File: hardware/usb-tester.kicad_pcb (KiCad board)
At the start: 2 copper layers, 32 parts, among them J1 TARGET, J10 Target 1, J11 USB1, J12 SWD2, J13 Target 2, J14 USB2, J15 SWD3, J16 Target 3, J17 USB3, J2 Comm, J3 CommLA, J4 PowerMon, J5 Upstream, J6 SWD0, J7 Target 0, J8 USB0, J9 SWD1, U1 TLV1117-33, U2 STMPS2151STR, U3 USBLC6-2SC6, U4 CD74HC4067SM, U5 4514, U6 FSUSB30MUX, U7 FSUSB30MUX

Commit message: WIP main board layout
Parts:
- R1, R2, R3, R4, R5, U5: moved to B.Cu
- moved R3 101.2 mm to (25.4, 125.7), turned to 180 degrees
- moved R5 93.2 mm to (25.4, 130.8)
- moved R4 84.1 mm to (25.4, 128.3), turned to 180 degrees
- moved R2 66.9 mm to (25.4, 113.0)
- moved J2 65.5 mm to (21.6, 108.0)
- moved J3 64.0 mm to (19.1, 108.0)
- moved U4 63.0 mm to (50.8, 125.9), turned to 180 degrees
- moved R1 60.4 mm to (25.4, 110.5)
- moved U5 54.8 mm to (55.2, 118.1)
- moved JP1 53.4 mm to (95.1, 60.1)
- moved C2 49.4 mm to (106.8, 58.2), turned to 180 degrees
- moved J14 35.8 mm to (66.0, 128.3)
- moved C1 33.4 mm to (102.5, 70.6)
- moved J4 32.4 mm to (117.1, 67.8)
- moved J17 30.8 mm to (81.3, 128.3)
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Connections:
- net Net-(C1-Pad1) renamed /VIN
- J1 pad 4: (no net) -> Net-(J1-Pad4)
- J5 pad 1: /USB_D+ -> GND
- J5 pad 3: GND -> /USB_D+
- U3 pad 1: /USB_D- -> /USB_D+
- U3 pad 3: /USB_D+ -> /USB_D-
- U3 pad 4: Net-(J1-Pad3) -> Net-(J1-Pad2)
- U3 pad 6: Net-(J1-Pad2) -> Net-(J1-Pad3)
- U4 pad 16: (no net) -> Net-(U4-Pad16)
- U4 pad 17: (no net) -> Net-(U4-Pad17)
- U4 pad 18: (no net) -> Net-(U4-Pad18)
- U4 pad 19: (no net) -> Net-(U4-Pad19)
- U4 pad 2: (no net) -> Net-(U4-Pad2)
- U4 pad 20: (no net) -> Net-(U4-Pad20)
- U4 pad 21: (no net) -> Net-(U4-Pad21)
- U4 pad 22: (no net) -> Net-(U4-Pad22)
- U4 pad 23: (no net) -> Net-(U4-Pad23)
- U4 pad 3: (no net) -> Net-(U4-Pad3)
- U4 pad 4: (no net) -> Net-(U4-Pad4)
- U4 pad 5: (no net) -> Net-(U4-Pad5)
- U5 pad 10: (no net) -> Net-(U5-Pad10)
- U5 pad 11: (no net) -> Net-(U5-Pad11)
- U5 pad 13: (no net) -> Net-(U5-Pad13)
- U5 pad 14: (no net) -> Net-(U5-Pad14)
- U5 pad 15: (no net) -> Net-(U5-Pad15)
- U5 pad 16: (no net) -> Net-(U5-Pad16)
- U5 pad 4: (no net) -> Net-(U5-Pad4)
- U5 pad 5: (no net) -> Net-(U5-Pad5)
- U5 pad 6: (no net) -> Net-(U5-Pad6)
- U5 pad 7: (no net) -> Net-(U5-Pad7)
- U5 pad 8: (no net) -> Net-(U5-Pad8)
- U5 pad 9: (no net) -> Net-(U5-Pad9)
- U6 pad 1: /SEL0 -> /USBSEL
- U7 pad 1: /SEL0 -> /USBSEL
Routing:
- net GND: track 3.81 -> 106.5 mm
- net /T_BOOT0: track 0.00 -> 54.5 mm
- net /T_RX: track 0.00 -> 54.0 mm
- net /T_VCC: track 0.00 -> 42.7 mm, vias 0 -> 1
- net /T3_TX: track 0.00 -> 29.5 mm
- net /T3_NRST: track 0.00 -> 27.9 mm
- net /USB_D+: track 0.00 -> 26.7 mm
- net /USB_D-: track 0.00 -> 26.3 mm
- net /T1_NRST: track 0.00 -> 23.4 mm, vias 0 -> 2
- net /USBSEL: track 0.00 -> 23.0 mm, vias 0 -> 2
- net /T1_TX: track 0.00 -> 19.9 mm, vias 0 -> 1
- net /T1_USB_D+: track 0.00 -> 19.4 mm, vias 0 -> 1
- net /T1_USB_D-: track 0.00 -> 19.3 mm, vias 0 -> 1
- net /T0_USB_D+: track 0.00 -> 15.5 mm, vias 0 -> 1
- net /T0_USB_D-: track 0.00 -> 15.5 mm, vias 0 -> 1
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
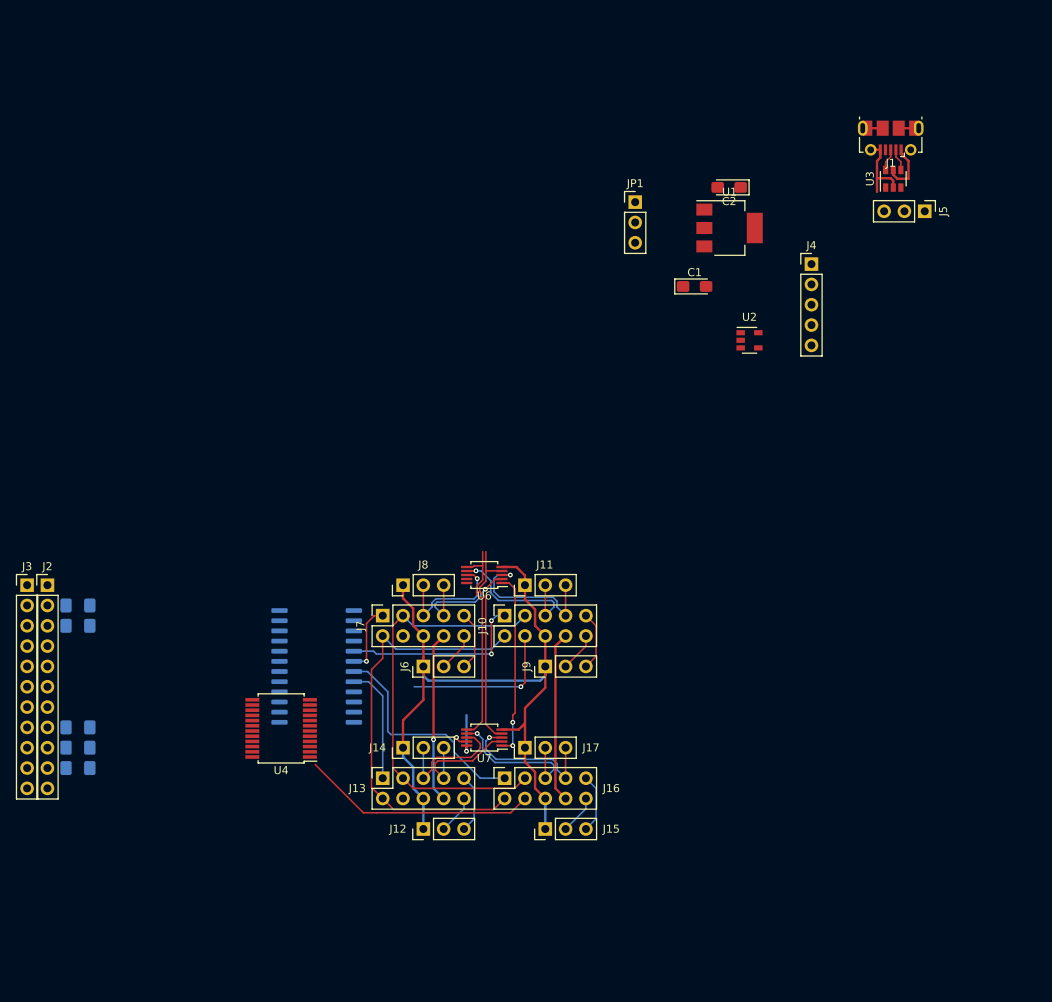
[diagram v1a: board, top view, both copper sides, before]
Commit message: Simplify schematics, add WIP layout
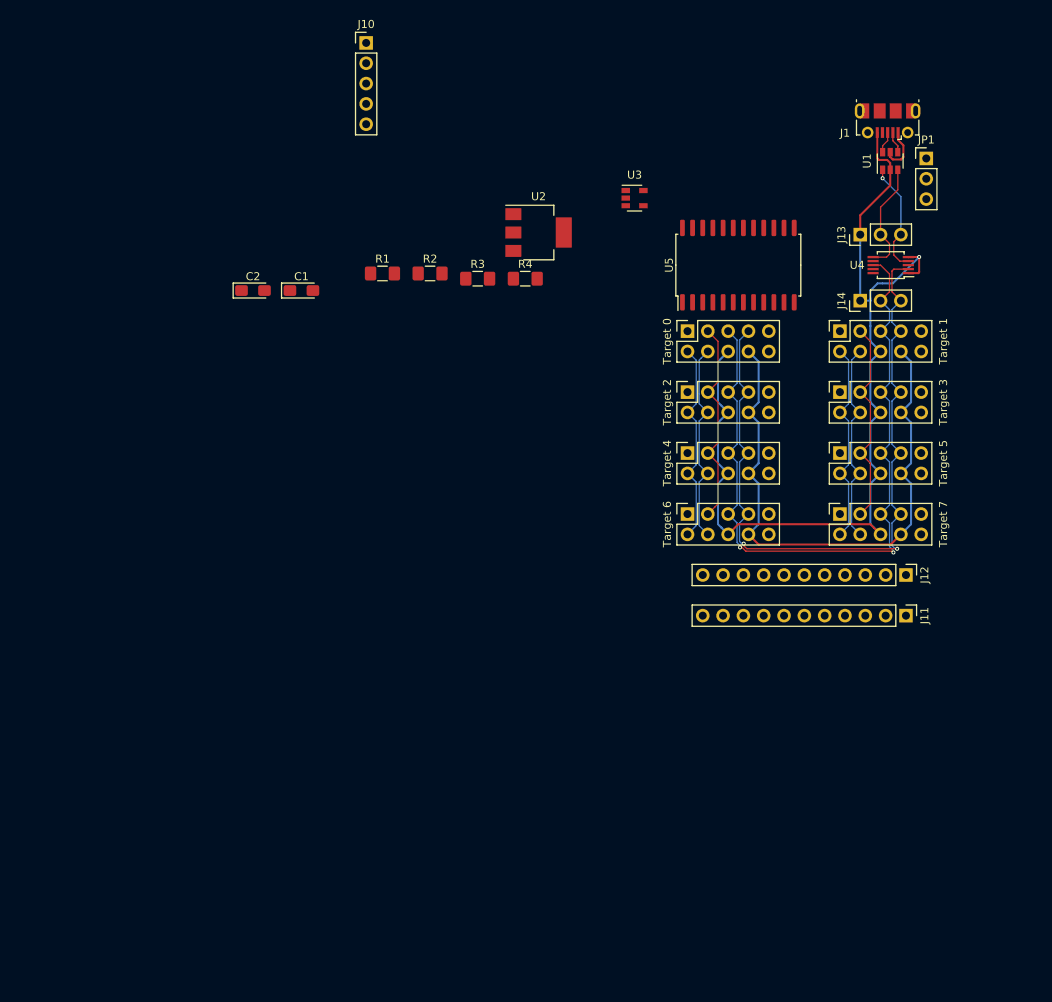
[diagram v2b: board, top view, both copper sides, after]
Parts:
- removed J15: SWD3, Connector_PinHeader_2.54mm:PinHeader_1x03_P2.54mm_Vertical
- removed J16: Target 3, Connector_PinSocket_2.54mm:PinSocket_2x05_P2.54mm_Vertical
- removed J17: USB3, Connector_PinHeader_2.54mm:PinHeader_1x03_P2.54mm_Vertical
- removed R5: 10k, Resistor_SMD:R_1206_3216Metric_Pad1.42x1.75mm_HandSolder
- removed U6, U7: FSUSB30MUX, Package_SO:MSOP-10_3x3mm_P0.5mm
- J10: value Target 1 -> PowerMon; footprint Connector_PinSocket_2.54mm:PinSocket_2x05_P2.54mm_Vertical -> Connector_PinHeader_2.54mm:PinHeader_1x05_P2.54mm_Vertical
- J11: value USB1 -> Comm; footprint Connector_PinHeader_2.54mm:PinHeader_1x03_P2.54mm_Vertical -> Connector_PinHeader_2.54mm:PinHeader_1x11_P2.54mm_Vertical
- J12: value SWD2 -> CommLA; footprint Connector_PinHeader_2.54mm:PinHeader_1x03_P2.54mm_Vertical -> Connector_PinHeader_2.54mm:PinHeader_1x11_P2.54mm_Vertical
- J13: value Target 2 -> Upstream; footprint Connector_PinSocket_2.54mm:PinSocket_2x05_P2.54mm_Vertical -> Connector_PinHeader_2.54mm:PinHeader_1x03_P2.54mm_Vertical
- J14: value USB2 -> Target
- J2: value Comm -> Target 0; footprint Connector_PinHeader_2.54mm:PinHeader_1x11_P2.54mm_Vertical -> Connector_PinSocket_2.54mm:PinSocket_2x05_P2.54mm_Vertical
- J3: value CommLA -> Target 1; footprint Connector_PinHeader_2.54mm:PinHeader_1x11_P2.54mm_Vertical -> Connector_PinSocket_2.54mm:PinSocket_2x05_P2.54mm_Vertical
- J4: value PowerMon -> Target 2; footprint Connector_PinHeader_2.54mm:PinHeader_1x05_P2.54mm_Vertical -> Connector_PinSocket_2.54mm:PinSocket_2x05_P2.54mm_Vertical
- J5: value Upstream -> Target 3; footprint Connector_PinHeader_2.54mm:PinHeader_1x03_P2.54mm_Vertical -> Connector_PinSocket_2.54mm:PinSocket_2x05_P2.54mm_Vertical
- J6: value SWD0 -> Target 4; footprint Connector_PinHeader_2.54mm:PinHeader_1x03_P2.54mm_Vertical -> Connector_PinSocket_2.54mm:PinSocket_2x05_P2.54mm_Vertical
- J7: value Target 0 -> Target 5
- J8: value USB0 -> Target 6; footprint Connector_PinHeader_2.54mm:PinHeader_1x03_P2.54mm_Vertical -> Connector_PinSocket_2.54mm:PinSocket_2x05_P2.54mm_Vertical
- J9: value SWD1 -> Target 7; footprint Connector_PinHeader_2.54mm:PinHeader_1x03_P2.54mm_Vertical -> Connector_PinSocket_2.54mm:PinSocket_2x05_P2.54mm_Vertical
- R1, R2, R3, R4: moved to F.Cu
- U1: value TLV1117-33 -> USBLC6-2SC6; footprint Package_TO_SOT_SMD:SOT-223-3_TabPin2 -> Package_TO_SOT_SMD:SOT-23-6
- U2: value STMPS2151STR -> TLV1117-33; footprint Package_TO_SOT_SMD:SOT-23-5 -> Package_TO_SOT_SMD:SOT-223-3_TabPin2
- U3: value USBLC6-2SC6 -> STMPS2151STR; footprint Package_TO_SOT_SMD:SOT-23-6 -> Package_TO_SOT_SMD:SOT-23-5
- U4: value CD74HC4067SM -> FSUSB30MUX; footprint Package_SO:SSOP-24_5.3x8.2mm_P0.65mm -> Package_SO:MSOP-10_3x3mm_P0.5mm
- U5: value 4514 -> 74HC4514D; moved to F.Cu
- moved J3 106.4 mm to (120.7, 76.2), turned to 90 degrees
- moved U4 95.7 mm to (127.0, 67.9)
- moved J13 90.4 mm to (123.2, 64.1)
- moved J2 86.1 mm to (101.6, 76.2), turned to 90 degrees
- moved R4 81.0 mm to (81.3, 69.6), turned to 0 degrees
- moved J14 79.9 mm to (123.2, 72.4)
- moved R3 75.1 mm to (75.4, 69.6), turned to 0 degrees
- moved J10 73.7 mm to (61.4, 40.2), turned to 0 degrees
- moved U5 72.8 mm to (108.0, 67.9), turned to 90 degrees
- moved J12 68.2 mm to (128.9, 106.7), turned to 270 degrees
- moved R2 62.3 mm to (69.4, 69.0)
- moved C2 60.9 mm to (47.3, 71.1), turned to 0 degrees
- moved J7 60.7 mm to (120.7, 91.4)
- moved R1 56.3 mm to (63.5, 69.0)
- moved C1 49.2 mm to (53.3, 71.1)
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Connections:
- J1 pad 2: Net-(J1-Pad2) -> /USBC_D-
- J1 pad 3: Net-(J1-Pad3) -> /USBC_D+
- J10 pad 1: /T1_NRST -> /T_VCC
- J10 pad 2: /T_BOOT0 -> /PWR_FAULT
- J10 pad 3: /T_RX -> /PWR_EN
- J10 pad 4: /T1_TX -> +3V3
- J10 pad 5: /T1_USB_D- -> GND
- J11 pad 2: /T1_USB_D- -> /T_BOOT0
- J11 pad 3: /T1_USB_D+ -> /T_NRST
- J12 pad 2: /T2_SWCLK -> /T_BOOT0
- J12 pad 3: /T2_SWDIO -> /T_NRST
- J13 pad 1: /T2_NRST -> GND
- J13 pad 2: /T_BOOT0 -> /USB_D-
- J13 pad 3: /T_RX -> /USB_D+
- J14 pad 2: /T2_USB_D- -> /T_USB_D-
- J14 pad 3: /T2_USB_D+ -> /T_USB_D+
- J2 pad 1: GND -> /T0_NRST
- J2 pad 10: /PWR_EN -> Net-(J2-Pad10)
- J2 pad 3: /T_NRST -> /T_RX
- J2 pad 5: /T_RX -> /T_USB_D-
- J2 pad 6: /SEL0 -> GND
- J2 pad 7: /SEL1 -> /T_USB_D+
- J2 pad 8: /USBMUXEN0 -> /T_VCC
- J2 pad 9: /USBMUXEN1 -> Net-(J2-Pad9)
- J3 pad 1: GND -> /T1_NRST
- J3 pad 10: /PWR_EN -> Net-(J3-Pad10)
- J3 pad 3: /T_NRST -> /T_RX
- J3 pad 5: /T_RX -> /T_USB_D-
- J3 pad 6: /SEL0 -> GND
- J3 pad 7: /SEL1 -> /T_USB_D+
- J3 pad 8: /USBMUXEN0 -> /T_VCC
- J3 pad 9: /USBMUXEN1 -> Net-(J3-Pad9)
- J4 pad 1: /T_VCC -> /T2_NRST
- J4 pad 2: /PWR_FAULT -> /T_BOOT0
- J4 pad 3: /PWR_EN -> /T_RX
- J4 pad 4: +3V3 -> /T_TX
- J4 pad 5: GND -> /T_USB_D-
- J5 pad 1: GND -> /T3_NRST
- J5 pad 2: /USB_D- -> /T_BOOT0
- J5 pad 3: /USB_D+ -> /T_RX
- J6 pad 1: GND -> /T4_NRST
- J6 pad 2: /T0_SWCLK -> /T_BOOT0
- J6 pad 3: /T0_SWDIO -> /T_RX
- J7 pad 1: /T0_NRST -> /T5_NRST
- J7 pad 10: /T0_SWCLK -> Net-(J7-Pad10)
- J7 pad 4: /T0_TX -> /T_TX
- J7 pad 5: /T0_USB_D- -> /T_USB_D-
- J7 pad 7: /T0_USB_D+ -> /T_USB_D+
- J7 pad 9: /T0_SWDIO -> Net-(J7-Pad9)
- J8 pad 1: GND -> /T6_NRST
- J8 pad 2: /T0_USB_D- -> /T_BOOT0
- J8 pad 3: /T0_USB_D+ -> /T_RX
- J9 pad 1: GND -> /T7_NRST
- J9 pad 2: /T1_SWCLK -> /T_BOOT0
- J9 pad 3: /T1_SWDIO -> /T_RX
- R1 pad 1: /T_BOOT0 -> GND
- R1 pad 2: +3V3 -> /PWR_EN
- R3 pad 1: +3V3 -> /T_BOOT0
- R3 pad 2: /USBMUXEN0 -> +3V3
- R4 pad 2: /USBMUXEN1 -> /~USBMUXEN
- U1 pad 1: GND -> /USB_D+
- U1 pad 2: +3V3 -> GND
- U1 pad 3: /VIN -> /USB_D-
- U2 pad 1: /T_VCC -> GND
- U2 pad 2: GND -> +3V3
- U2 pad 3: /PWR_FAULT -> /VIN
- U3 pad 1: /USB_D+ -> /T_VCC
- U3 pad 3: /USB_D- -> /PWR_FAULT
- U3 pad 4: Net-(J1-Pad2) -> /PWR_EN
- U3 pad 5: VBUS -> +3V3
- U4 pad 1: /T_TX -> GND
- U4 pad 10: /SEL0 -> +3V3
- U4 pad 2: Net-(U4-Pad2) -> /T_USB_D+
- U4 pad 4: Net-(U4-Pad4) -> /USB_D+
- U4 pad 5: Net-(U4-Pad5) -> GND
- U4 pad 6: /T3_TX -> /USB_D-
- U4 pad 7: /T2_TX -> Net-(U4-Pad7)
- U4 pad 8: /T1_TX -> /T_USB_D-
- U4 pad 9: /T0_TX -> /~USBMUXEN
- U5 pad 13: Net-(U5-Pad13) -> /T5_NRST
- U5 pad 14: Net-(U5-Pad14) -> /T4_NRST
- U5 pad 15: Net-(U5-Pad15) -> /T7_NRST
- U5 pad 16: Net-(U5-Pad16) -> /T6_NRST
- U5 pad 21: GND -> /SEL2
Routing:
- net /T_USB_D-: track 0.00 -> 92.0 mm, vias 0 -> 2
- net /T_USB_D+: track 0.00 -> 91.7 mm, vias 0 -> 2
- net /T_TX: track 0.00 -> 51.1 mm
- net /T3_TX: track 29.5 -> 0.00 mm
- net /T_VCC: track 42.7 -> 72.1 mm, vias 1 -> 0
- net /T3_NRST: track 27.9 -> 0.00 mm
- net /T1_NRST: track 23.4 -> 0.00 mm, vias 2 -> 0
- net /USBSEL: track 23.0 -> 0.00 mm, vias 2 -> 0
- net /T1_TX: track 19.9 -> 0.00 mm, vias 1 -> 0
- net /T1_USB_D+: track 19.4 -> 0.00 mm, vias 1 -> 0
- net /T1_USB_D-: track 19.3 -> 0.00 mm, vias 1 -> 0
- net /T3_USB_D+: track 18.9 -> 0.00 mm, vias 1 -> 0
- net /T3_USB_D-: track 18.8 -> 0.00 mm, vias 1 -> 0
- net /T2_USB_D-: track 15.6 -> 0.00 mm
- net /T2_USB_D+: track 15.6 -> 0.00 mm
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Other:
- net class Default: clearance 0.2 -> 0.1524; trace_width 0.2 -> 0.1524; via_dia 0.6 -> 0.508; via_drill 0.3 -> 0.254
- net class Power: clearance 0.2 -> 0.1524; trace_width 0.3 -> 0.254; via_dia 0.6 -> 0.508; via_drill 0.3 -> 0.254
- rule pad_to_mask_clearance: 0 -> 0.000051
- rule trace_clearance: 0.2 -> 0.1524
- rule trace_min: 0.2 -> 0.1524
- rule via_min_drill: 0.3 -> 0.254
- rule via_min_size: 0.4 -> 0.508

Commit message: Finalize shematics and layout
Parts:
- removed C1, C2: 10uF, Capacitor_Tantalum_SMD:CP_EIA-3216-18_Kemet-A_Pad1.58x1.35mm_HandSolder
- removed J10: PowerMon, Connector_PinHeader_2.54mm:PinHeader_1x05_P2.54mm_Vertical
- removed JP1: Power source, Connector_PinHeader_2.54mm:PinHeader_1x03_P2.54mm_Vertical
- removed U2: TLV1117-33, Package_TO_SOT_SMD:SOT-223-3_TabPin2
- added J15: Idd, Connector_PinHeader_2.54mm:PinHeader_1x02_P2.54mm_Vertical, F.Cu at (109.2, 69.8)
- moved R1 55.5 mm to (118.9, 72.4), turned to 180 degrees
- moved R3 51.9 mm to (116.2, 101.6), turned to 180 degrees
- moved J11 51.7 mm to (91.4, 76.2), turned to 0 degrees
- moved J12 46.4 mm to (94.0, 76.2), turned to 0 degrees
- moved R4 39.7 mm to (120.9, 67.3)
- moved R2 26.0 mm to (94.0, 60.5), turned to 180 degrees
- moved U3 21.4 mm to (113.0, 71.1)
- moved J1 18.6 mm to (111.8, 61.1)
- moved U1 15.9 mm to (115.6, 66.0), turned to 180 degrees
- moved U5 9.53 mm to (98.4, 67.8)
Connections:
- net VBUS renamed /VBUS
- J11 pad 1: GND -> +3V3
- J11 pad 10: /PWR_EN -> /T_TX
- J11 pad 11: /EXT_5V -> /T_BOOT0
- J11 pad 2: /T_BOOT0 -> GND
- J11 pad 4: /T_TX -> /SEL0
- J11 pad 5: /T_RX -> /SEL1
- J11 pad 6: /SEL0 -> /SEL2
- J11 pad 7: /SEL1 -> /~USBMUXEN
- J11 pad 8: /SEL2 -> /PWR_EN
- J11 pad 9: /~USBMUXEN -> /T_RX
- J12 pad 1: GND -> +3V3
- J12 pad 10: /PWR_EN -> /T_TX
- J12 pad 11: /EXT_5V -> /T_BOOT0
- J12 pad 2: /T_BOOT0 -> GND
- J12 pad 4: /T_TX -> /SEL0
- J12 pad 5: /T_RX -> /SEL1
- J12 pad 6: /SEL0 -> /SEL2
- J12 pad 7: /SEL1 -> /~USBMUXEN
- J12 pad 8: /SEL2 -> /PWR_EN
- J12 pad 9: /~USBMUXEN -> /T_RX
- R3 pad 2: +3V3 -> /T_VCC
- U3 pad 1: /T_VCC -> /T_VCC_SRC
- U5 pad 13: /T5_NRST -> /T1_NRST
- U5 pad 14: /T4_NRST -> /T3_NRST
- U5 pad 15: /T7_NRST -> /T5_NRST
- U5 pad 16: /T6_NRST -> /T7_NRST
- U5 pad 17: /T1_NRST -> /T0_NRST
- U5 pad 18: /T0_NRST -> /T2_NRST
- U5 pad 19: /T3_NRST -> /T4_NRST
- U5 pad 20: /T2_NRST -> /T6_NRST
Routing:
- net GND: track 117.9 -> 181.9 mm, vias 1 -> 3
- net +3V3: track 0.00 -> 58.8 mm
- net /~USBMUXEN: track 0.00 -> 55.6 mm, vias 0 -> 1
- net /PWR_EN: track 0.00 -> 51.5 mm, vias 0 -> 1
- net /T7_NRST: track 0.00 -> 47.4 mm, vias 0 -> 1
- net /T5_NRST: track 0.00 -> 38.9 mm, vias 0 -> 1
- net /T6_NRST: track 0.00 -> 38.6 mm, vias 0 -> 1
- net /T_TX: track 51.1 -> 86.2 mm
- net /T_BOOT0: track 51.1 -> 85.0 mm, vias 0 -> 1
- net /T_RX: track 52.0 -> 84.1 mm
- net /T3_NRST: track 0.00 -> 30.6 mm, vias 0 -> 1
- net /T4_NRST: track 0.00 -> 30.4 mm, vias 0 -> 1
- net /SEL2: track 0.00 -> 29.2 mm, vias 0 -> 1
- net /T_NRST: track 0.00 -> 26.7 mm, vias 0 -> 1
- net /T2_NRST: track 0.00 -> 22.3 mm, vias 0 -> 1
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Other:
- board outline added: 45.1 x 47 mm
- board text added: "3V3"
- board text added: "BT0"
- board text added: "GND"
- board text added: "PEN"
- board text added: "RX"
- board text added: "S0"
- board text added: "S1"
- board text added: "S2"
- board text added: "TX"
- board text added: "~RST"
- board text added: "~UEN"

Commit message: Re-import netlist
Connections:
- net /PWR_FAULT renamed Net-(U3-Pad3)

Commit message: Update design rules
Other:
- rule pad_to_mask_clearance: 0.000051 -> 0.0508
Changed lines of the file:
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@@
     (pad_size 1.524 1.524)
     (pad_drill 0.762)
-    (pad_to_mask_clearance 0.000051)
+    (pad_to_mask_clearance 0.0508)
+    (solder_mask_min_width 0.1016)
     (aux_axis_origin 0 0)
     (visible_elements FFFFFF7F)

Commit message: Update layout
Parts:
- J2, J3, J4, J5, J6, J7, J8, J9: footprint Connector_PinSocket_2.54mm:PinSocket_2x05_P2.54mm_Vertical -> unsorted:PinSocket_2x05_P2.54mm_Vertical_Reversed
- moved R3 7.65 mm to (121.9, 96.5), turned to 0 degrees
- moved J4 2.54 mm to (101.6, 86.4)
- moved J5 2.54 mm to (120.7, 86.4)
- moved J6 2.54 mm to (101.6, 94.0)
- moved J7 2.54 mm to (120.7, 94.0)
- moved J2 2.54 mm to (101.6, 78.7)
- moved J3 2.54 mm to (120.7, 78.7)
- moved J8 2.54 mm to (101.6, 101.6)
- moved J9 2.54 mm to (120.7, 101.6)
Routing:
- net /T_TX: track 86.2 -> 93.1 mm, vias 0 -> 1
- net /T_BOOT0: track 85.0 -> 91.8 mm, vias 1 -> 0
- net /T6_NRST: track 38.6 -> 42.8 mm
- net /T3_NRST: track 30.6 -> 34.7 mm
- net /T5_NRST: track 38.9 -> 42.8 mm
- net /T0_NRST: track 13.6 -> 17.5 mm
- net /T1_NRST: track 22.2 -> 25.5 mm
- net /T7_NRST: track 47.4 -> 50.6 mm
- net /T_VCC: track 80.8 -> 83.6 mm
- net /T2_NRST: track 22.3 -> 25.0 mm
- net /T4_NRST: track 30.4 -> 33.1 mm
- net GND: track 181.9 -> 179.9 mm, vias 3 -> 2
- net /T_USB_D-: track 92.0 -> 90.3 mm, vias 2 -> 0
- net /T_USB_D+: track 91.7 -> 90.3 mm, vias 2 -> 0
- net /T_RX: track 84.1 -> 85.1 mm
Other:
- board size 45.1 x 47 mm -> 44.5 x 46.4 mm
- board text added: "BOOT0"
- board text added: "PWR_EN"
- board text added: "SEL0"
- board text added: "SEL1"
- board text added: "SEL2"
- board text added: "~RESET"
- board text added: "~USB_EN"
- board text removed: "BT0"
- board text removed: "PEN"
- board text removed: "S0"
- board text removed: "S1"
- board text removed: "S2"
- board text removed: "~RST"
- board text removed: "~UEN"

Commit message: Add labels
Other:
- board text added: "D+"
- board text added: "D-"
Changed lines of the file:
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@@
   (general
     (thickness 1.6)
-    (drawings 15)
+    (drawings 18)
     (tracks 496)
     (zones 0)
@@
     (solder_mask_min_width 0.1016)
     (aux_axis_origin 0 0)
-    (visible_elements FFF9FF7F)
+    (visible_elements FFFFFF7F)
     (pcbplotparams
       (layerselection 0x010fc_ffffffff)
@@
     (descr "Through hole straight pin header, 1x02, 2.54mm pitch, single row")
     (tags "Through hole pin header THT 1x02 2.54mm single row")
-    (fp_text reference J15 (at 0 -2.33) (layer F.SilkS)
-      (effects (font (size 1 1) (thickness 0.15)))
-    )
-    (fp_text value Idd (at 0 4.87) (layer F.Fab)
+    (fp_text reference J15 (at 0 -2.33) (layer F.Fab)
+      (effects (font (size 1 1) (thickness 0.15)))
+    )
+    (fp_text value Idd (at 0 -2.286) (layer F.SilkS)
       (effects (font (size 1 1) (thickness 0.15)))
     )
@@
     )
   )
+  (gr_text D+ (at 128.524 61.722) (layer F.SilkS)
+    (effects (font (size 0.8 0.8) (thickness 0.15)))
+  )
+  (gr_text D- (at 125.984 61.722) (layer F.SilkS)
+    (effects (font (size 0.8 0.8) (thickness 0.15)))
+  )
+  (gr_text GND (at 123.19 61.722) (layer F.SilkS)
+    (effects (font (size 0.8 0.8) (thickness 0.15)))
+  )
   (gr_text BOOT0 (at 97.409 101.6) (layer F.SilkS)

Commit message: Tune silkscreen params a little bit
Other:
- rule pad_to_mask_clearance: 0.0508 -> 0.045
- rule solder_mask_min_width: 0.1016 -> 0.101
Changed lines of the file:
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@@
     (pad_size 1.524 1.524)
     (pad_drill 0.762)
-    (pad_to_mask_clearance 0.0508)
-    (solder_mask_min_width 0.1016)
+    (pad_to_mask_clearance 0.045)
+    (solder_mask_min_width 0.101)
     (aux_axis_origin 0 0)
     (visible_elements FFFFFF7F)
     (pcbplotparams
-      (layerselection 0x010fc_ffffffff)
+      (layerselection 0x010f0_ffffffff)
       (usegerberextensions false)
       (usegerberattributes false)
@@
       (padsonsilk false)
       (subtractmaskfromsilk false)
-      (outputformat 4)
+      (outputformat 1)
       (mirror false)
       (drillshape 0)
